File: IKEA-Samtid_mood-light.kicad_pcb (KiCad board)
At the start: 2 copper layers, 100 x 100 mm, 143 parts, among them P2 POWER, P3.1 B-to-B-1A, P4.1 B-to-B-2A, Q1 BSS138, Q2 BSS138, Q3 IRLML6401PbF, Q4 IRLML6401PbF

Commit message: Being creative...
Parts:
- removed DS1: DIODESCH, my_parts:MADW__diode_sub-SMA
- added REF**: HC-06, Bluetooth:HC-06, F.Cu at (120.8, 96.1)
- added U1: AP2204K-SOT23-5, my_parts:MADW__SOT23-5, B.Cu at (150.0, 68.0)
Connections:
- net /TXO/LEDs renamed /LEDS.A
- net Net-(P4.1-Pad1) renamed /RXI.A
- net Net-(P4.1-Pad3) renamed /TXO.A
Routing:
- net +5V: track 627.0 -> 630.8 mm
- net /WS2812B-LEDs-1/GND: track 632.5 -> 633.9 mm, vias 36 -> 37
- net /VCC.A: track 16.6 -> 17.1 mm
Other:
- outline, holes or cut-outs redrawn
- board text added: "IKEA-Samtid mood-light V0.40.a 2015 - blog.spitzenpfeil.org"
- board text removed: "IKEA-Samtid mood-light V0.31.c 2015 - blog.spitzenpfeil.org"

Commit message: Switched to SIL-6 connector for HC-05 (vertically mounted).
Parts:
- removed REF**: HC-06, Bluetooth:HC-06
- added Radio1: HC-05 (vert.), my_parts:MADW__SIL-6, F.Cu at (150.1, 59.5)
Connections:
- P4.1 pad 1: /RXI.A -> Net-(P4.1-Pad1)
- P4.1 pad 2: Net-(P4.1-Pad2) -> /RXI.A
- P4.1 pad 3: /TXO.A -> Net-(P4.1-Pad3)
- P4.1 pad 4: Net-(P4.1-Pad4) -> /TXO.A
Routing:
- net /VCC.A: track 17.1 -> 31.1 mm
- net /RXI.A: track 0.00 -> 13.8 mm
- net /TXO.A: track 0.00 -> 10.2 mm
- net /WS2812B-LEDs-1/A_IN: track 28.9 -> 29.7 mm

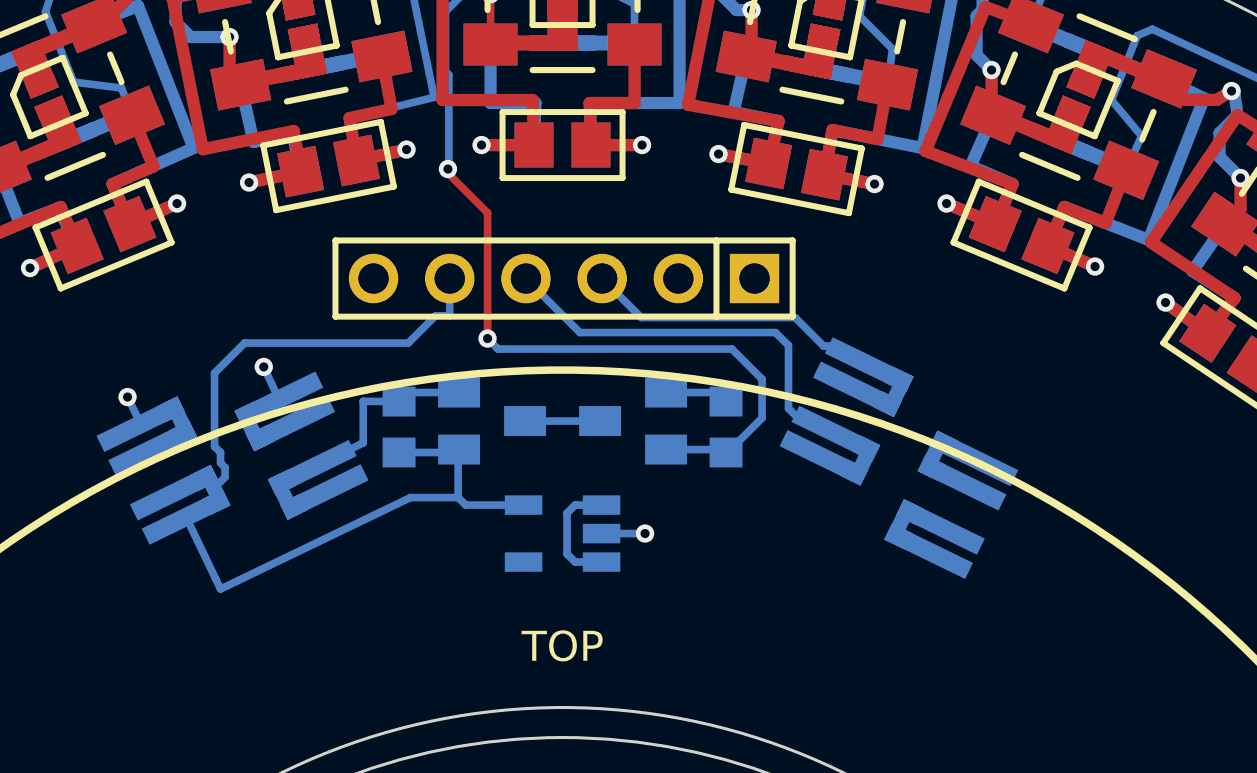
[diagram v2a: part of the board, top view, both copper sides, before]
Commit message: Added decoupling cap for 3.3V reg.
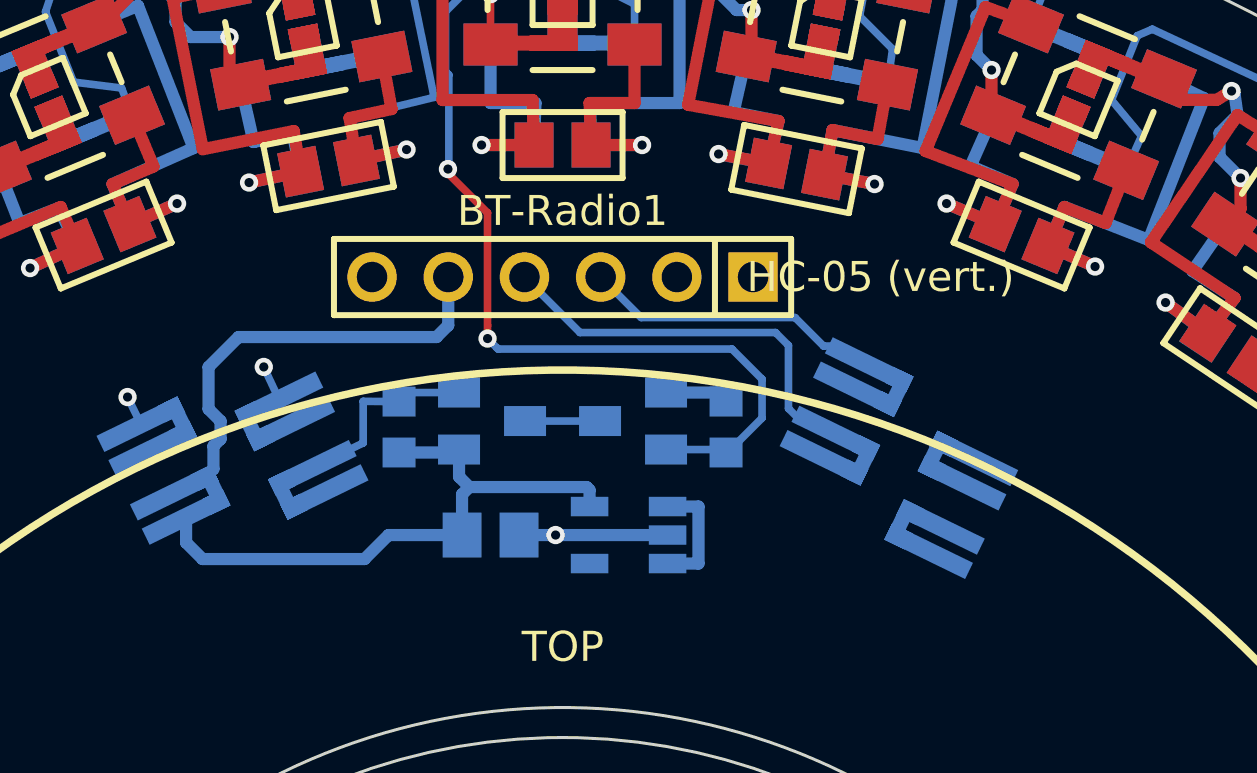
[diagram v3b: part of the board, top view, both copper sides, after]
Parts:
- added C3: 1µ, my_parts:MADW__C0805, B.Cu at (147.6, 68.0)
- moved U1 2.20 mm to (152.2, 68.0)
- moved BT-Radio1 0.07 mm to (150.0, 59.4)
- renumbered Radio1 to BT-Radio1
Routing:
- net /VCC.A: track 31.1 -> 34.6 mm
- net /WS2812B-LEDs-1/GND: track 633.9 -> 637.4 mm

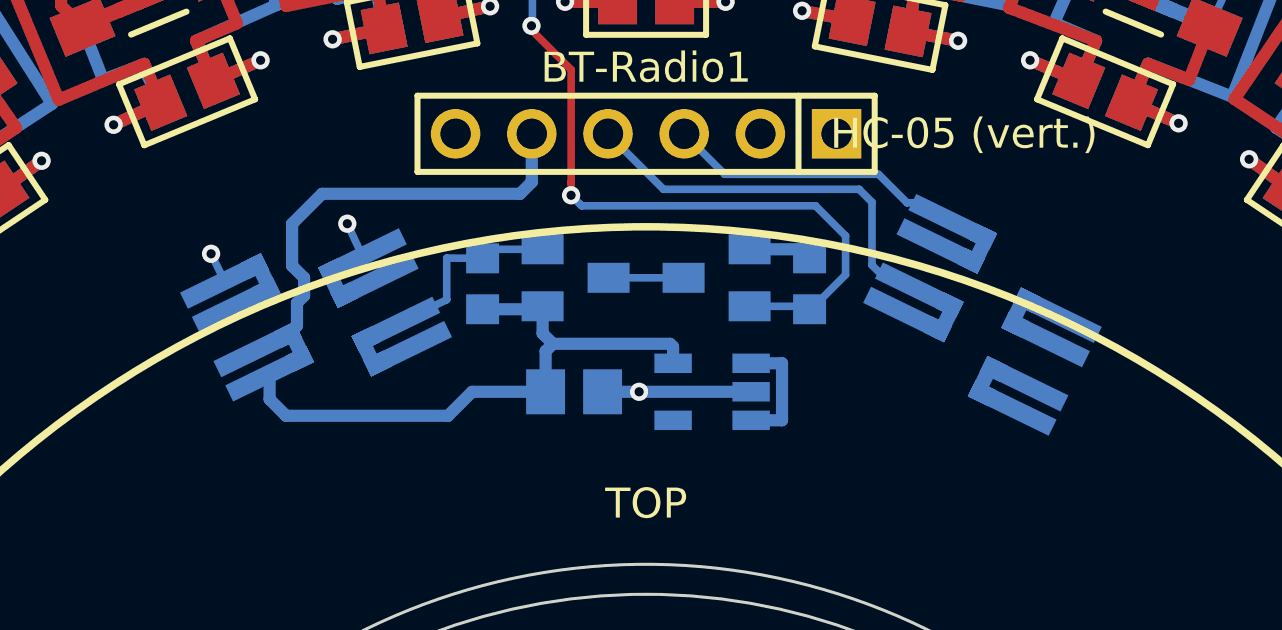
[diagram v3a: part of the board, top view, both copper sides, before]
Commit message: 180-d the microMaTch connectors to prevent plugging in old boards.
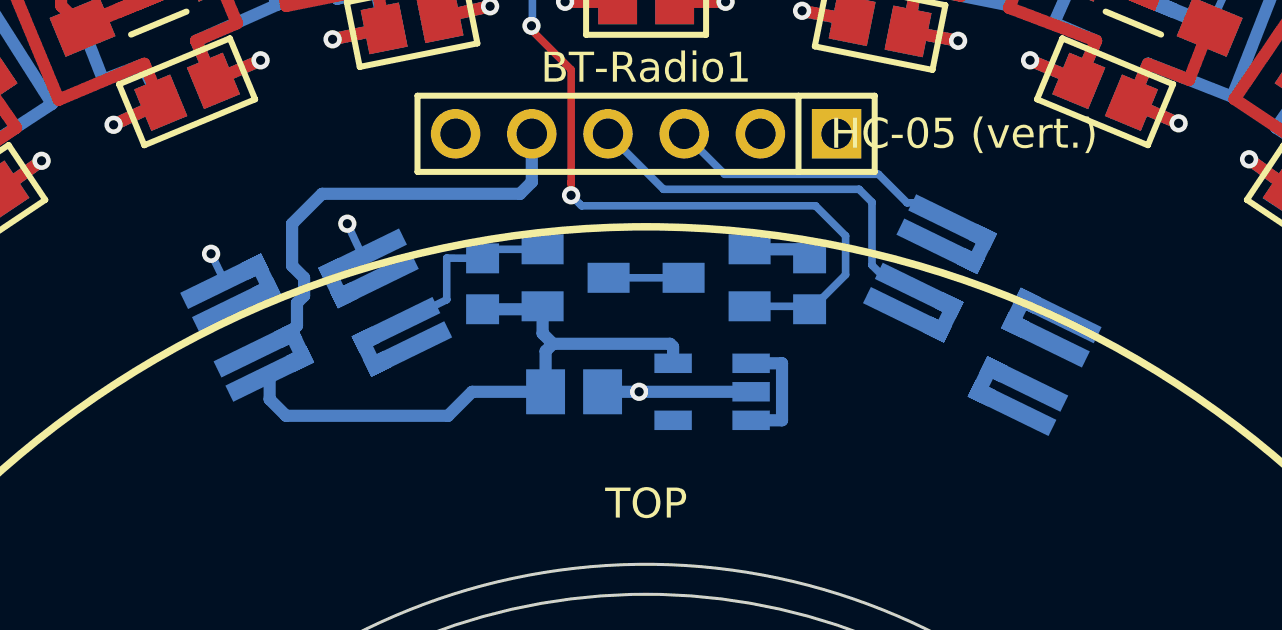
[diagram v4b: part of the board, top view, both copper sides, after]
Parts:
- turned P3.1 to 116 degrees
- turned P4.1 to 64 degrees
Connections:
- P3.1 pad 1: /LEDS.A -> /WS2812B-LEDs-1/GND
- P3.1 pad 2: /VCC.A -> /WS2812B-LEDs-1/GND
- P3.1 pad 3: /WS2812B-LEDs-1/GND -> /VCC.A
- P3.1 pad 4: /WS2812B-LEDs-1/GND -> /LEDS.A
- P4.1 pad 1: Net-(P4.1-Pad1) -> /TXO.A
- P4.1 pad 2: /RXI.A -> Net-(P4.1-Pad2)
- P4.1 pad 3: Net-(P4.1-Pad3) -> /RXI.A
- P4.1 pad 4: /TXO.A -> Net-(P4.1-Pad4)

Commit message: Playing with HC-05 placement.
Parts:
- BT-Radio1: value HC-05 (vert.) -> HC-05; footprint my_parts:MADW__SIL-6 -> SIL-Headers:SIL-7
- moved BT-Radio1 1.07 mm to (148.9, 59.5)
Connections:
- P3.1 pad 2: /WS2812B-LEDs-1/GND -> /DTR.A
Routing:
- net /DTR.A: track 0.00 -> 4.66 mm, vias 0 -> 1
- net /WS2812B-LEDs-1/GND: track 637.4 -> 636.2 mm, vias 37 -> 36
- net /VCC.A: track 34.6 -> 33.6 mm

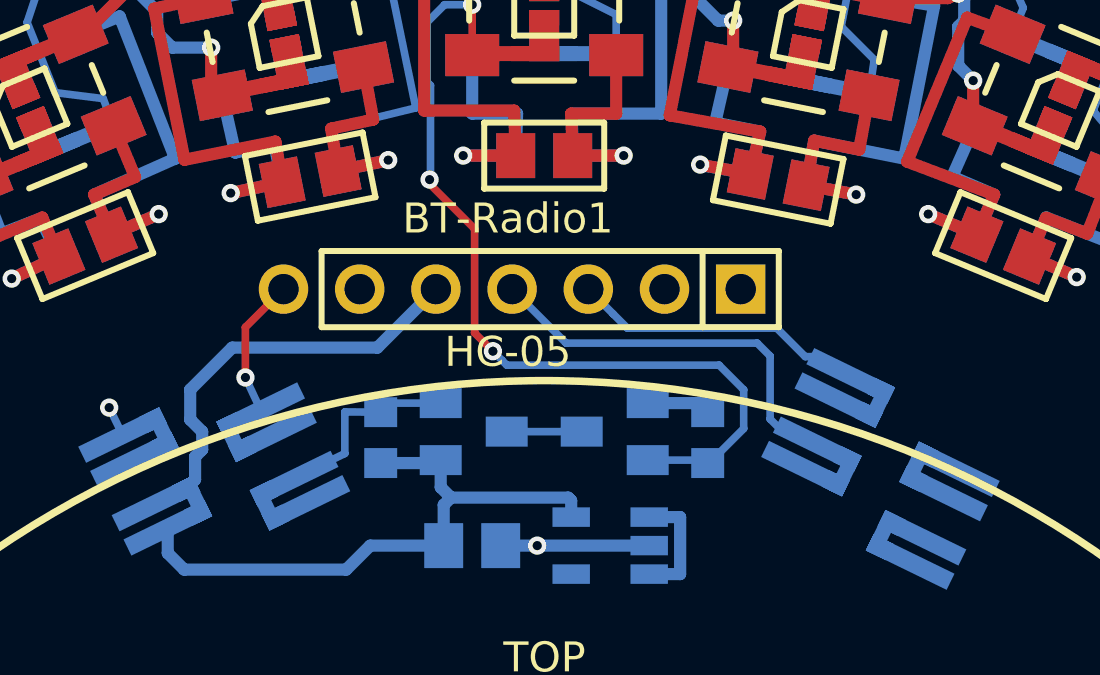
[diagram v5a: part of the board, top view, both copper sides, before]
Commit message: HC-05 tweaks. Forgot about on-board 3.3V regulator.
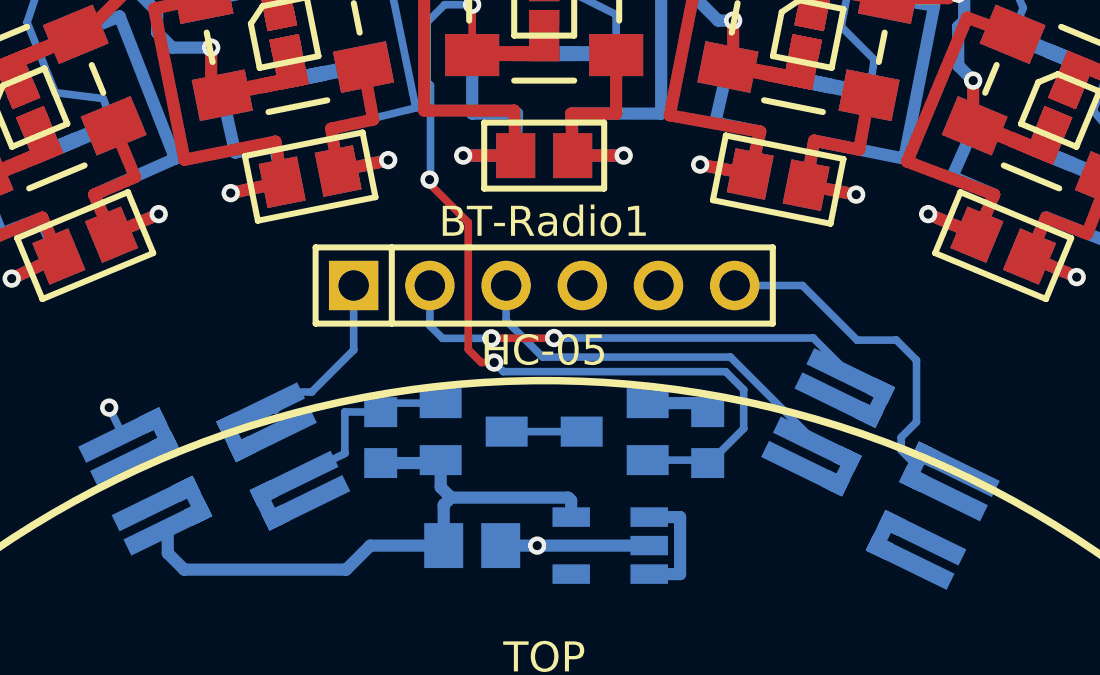
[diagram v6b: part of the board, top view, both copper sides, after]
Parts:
- BT-Radio1: footprint SIL-Headers:SIL-7 -> SIL-Headers:SIL-6
- moved BT-Radio1 1.08 mm to (150.0, 59.3), turned to 0 degrees
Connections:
- BT-Radio1 pad 1: (no net) -> /DTR.A
- BT-Radio1 pad 2: (no net) -> /TXO.A
- BT-Radio1 pad 3: /TXO.A -> /RXI.A
- BT-Radio1 pad 4: /RXI.A -> /WS2812B-LEDs-1/GND
- BT-Radio1 pad 5: /VCC.A -> +5V
- BT-Radio1 pad 6: /WS2812B-LEDs-1/GND -> /KEY.A
- P4.1 pad 2: Net-(P4.1-Pad2) -> /KEY.A
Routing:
- net /VCC.A: track 33.6 -> 20.4 mm
- net /KEY.A: track 0.00 -> 11.0 mm
- net /TXO.A: track 10.0 -> 16.1 mm, vias 0 -> 2
- net /DTR.A: track 4.66 -> 6.08 mm, vias 1 -> 0

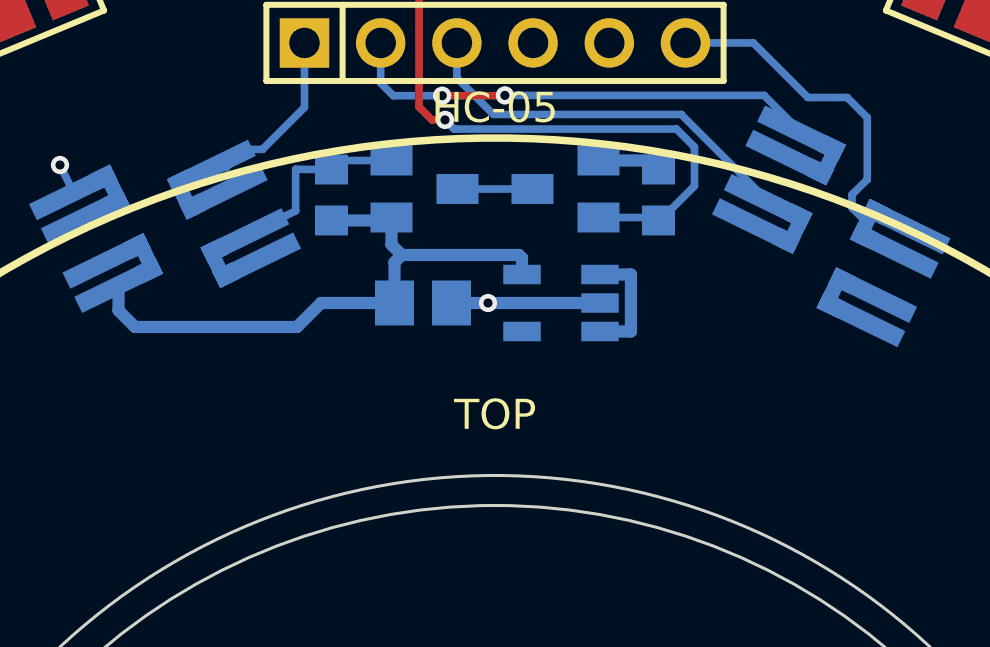
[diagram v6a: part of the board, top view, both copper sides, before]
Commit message: Added info for alternative 3.3V regulator.
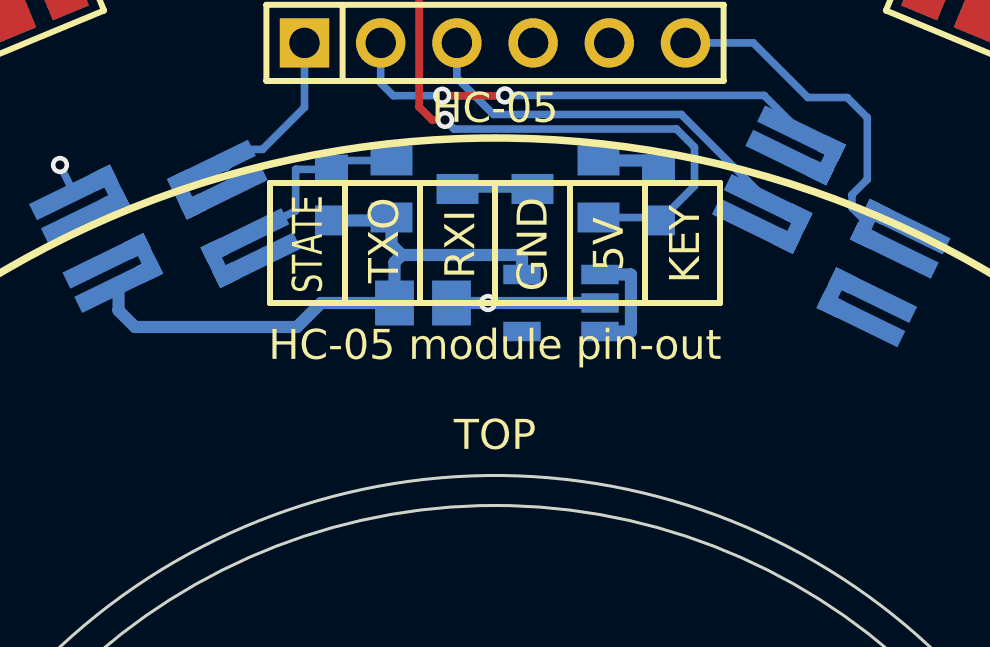
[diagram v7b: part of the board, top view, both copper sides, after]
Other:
- board text added: "GND"
- board text added: "HC-05 module pin-out"
- board text added: "KEY"
- board text added: "RXI"
- board text added: "STATE"
- board text added: "TXO"

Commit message: Tweaks.
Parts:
- BT-Radio1: value HC-05 -> HC-05 [JY-MCU]
